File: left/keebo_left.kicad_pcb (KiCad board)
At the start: 2 copper layers, 152.4 x 100 mm, 58 parts, among them J1 Conn_01x05, J2 Conn_01x08, SW1 SW_Push, SW10 SW_Push, SW11 SW_Push, SW12 SW_Push, SW13 SW_Push, SW14 SW_Push, SW17 SW_Push, SW18 SW_Push, SW19 SW_Push, SW2 SW_Push, SW20 SW_Push, SW21 SW_Push, SW22 SW_Push, SW25 SW_Push, SW26 SW_Push, SW27 SW_Push, SW28 SW_Push, SW29 SW_Push, SW3 SW_Push, SW30 SW_Push, SW35 SW_Push, SW36 SW_Push, SW37 SW_Push, SW4 SW_Push, SW5 SW_Push, SW6 SW_Push, SW7 SW_Push, SW9 SW_Push

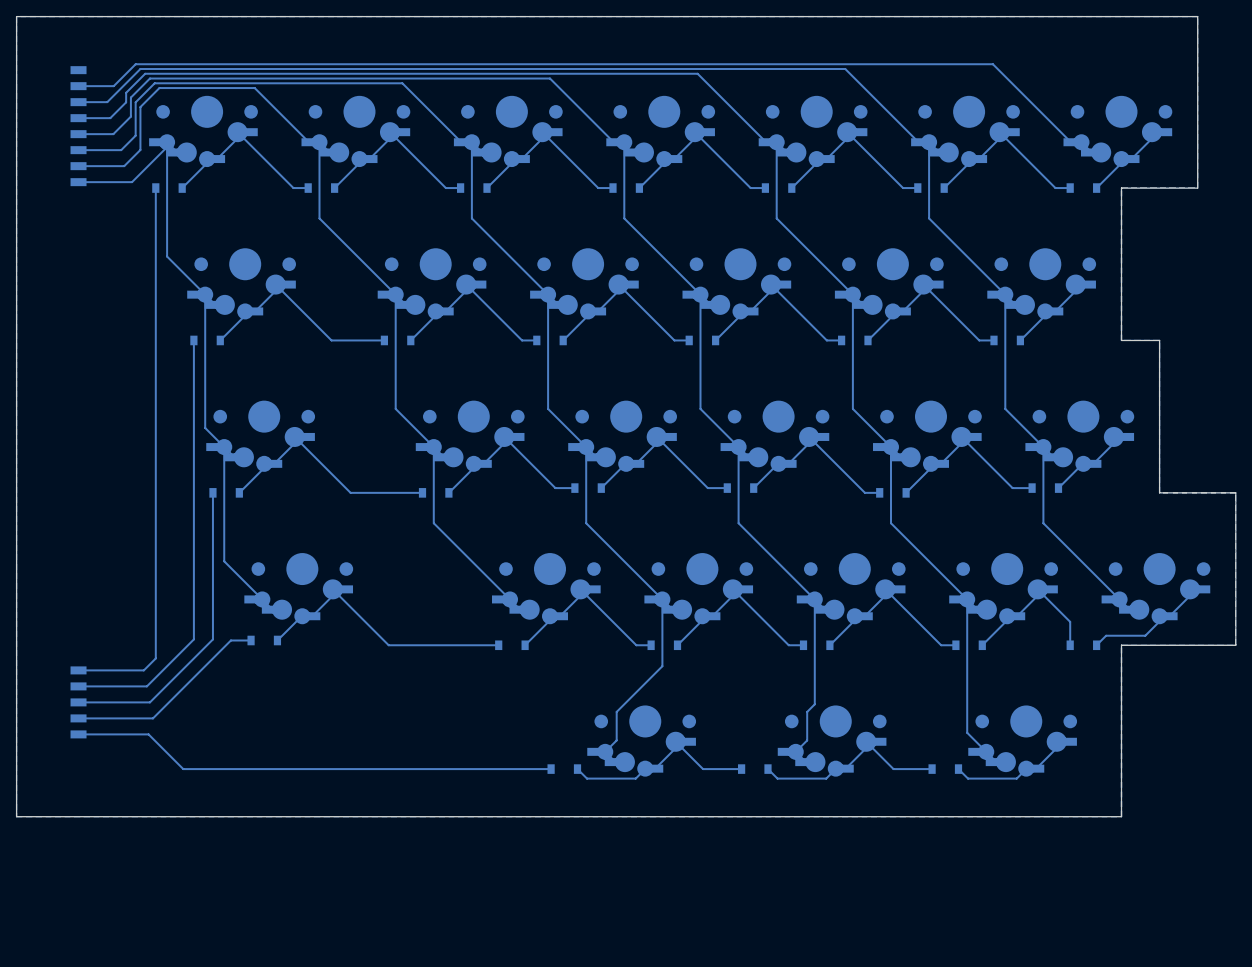
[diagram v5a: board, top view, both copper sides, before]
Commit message: Fix key matrix; use MX exclusively; Fix MX missing side holes.
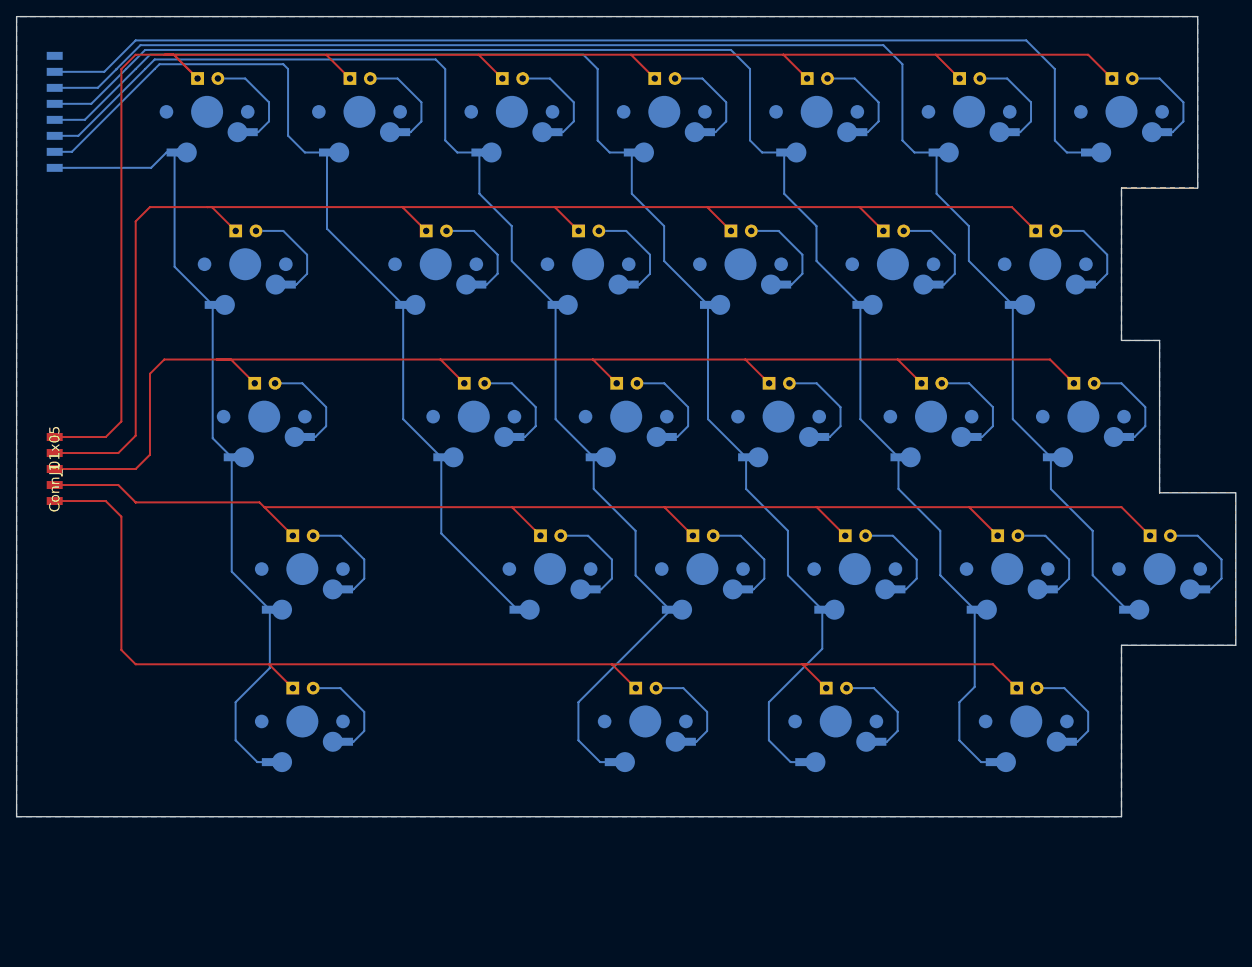
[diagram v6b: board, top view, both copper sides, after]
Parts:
- added D33: 1N4148, Diodes_THT:D_DO-35_SOD27_P2.54mm_Vertical_AnodeUp, B.Cu at (53.6, 103.0)
- added SW33: SW_Push, kbo_mx_3d:KeeboHR_125_MX, B.Cu at (54.8, 107.2)
- D1, D10, D11, D12, D13, D14, D17, D18, D19, D2, D20, D21, D22, D25, D26, D27, D28, D29, D3, D30, D35, D36, D37, D4, D5, D6, D7, D9: footprint Diodes_SMD:D_SOD-123 -> Diodes_THT:D_DO-35_SOD27_P2.54mm_Vertical_AnodeUp
- J1: moved to F.Cu
- SW1, SW10, SW11, SW12, SW13, SW14, SW18, SW19, SW2, SW20, SW21, SW22, SW26, SW27, SW28, SW29, SW3, SW30, SW4, SW5, SW6, SW7: footprint kbo_mx_lp_3d:KeeboHR_100_MX_LP -> kbo_mx_3d:KeeboHR_100_MX
- SW17: footprint kbo_mx_lp_3d:KeeboHR_175_MX_LP -> kbo_mx_3d:KeeboHR_175_MX
- SW25: footprint kbo_mx_lp_3d:KeeboHR_225_MX_LP -> kbo_mx_3d:KeeboHR_225_MX
- SW35, SW36, SW37: footprint kbo_mx_lp_3d:KeeboHR_125_MX_LP -> kbo_mx_3d:KeeboHR_125_MX
- SW9: footprint kbo_mx_lp_3d:KeeboHR_150_MX_LP -> kbo_mx_3d:KeeboHR_150_MX
- moved J1 29.3 mm to (23.8, 75.6)
- moved D30 16.0 mm to (160.7, 83.9)
- moved D1 14.2 mm to (41.7, 26.8)
- moved D2 14.2 mm to (60.7, 26.8)
- moved D3 14.2 mm to (79.8, 26.8)
- moved D5 14.2 mm to (117.9, 26.8)
- moved D6 14.2 mm to (136.9, 26.8)
- moved D7 14.2 mm to (156.0, 26.8)
- moved D4 14.2 mm to (98.8, 26.8)
- moved D11 14.2 mm to (89.3, 45.8)
- moved D12 14.2 mm to (108.3, 45.8)
- moved D13 14.2 mm to (127.4, 45.8)
- moved D14 14.2 mm to (146.4, 45.8)
- moved D17 14.2 mm to (48.8, 64.9)
- moved D9 14.2 mm to (46.4, 45.8)
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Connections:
- D10 pad 1: Net-(D10-Pad1) -> /row2
- D11 pad 1: Net-(D10-Pad2) -> /row2
- D12 pad 1: Net-(D11-Pad2) -> /row2
- D13 pad 1: Net-(D12-Pad2) -> /row2
- D14 pad 1: Net-(D13-Pad2) -> /row2
- D18 pad 1: Net-(D17-Pad2) -> /row3
- D19 pad 1: Net-(D18-Pad2) -> /row3
- D2 pad 1: Net-(D1-Pad2) -> /row1
- D20 pad 1: Net-(D19-Pad2) -> /row3
- D21 pad 1: Net-(D20-Pad2) -> /row3
- D22 pad 1: Net-(D21-Pad2) -> /row3
- D26 pad 1: Net-(D25-Pad2) -> /row4
- D27 pad 1: Net-(D26-Pad2) -> /row4
- D28 pad 1: Net-(D27-Pad2) -> /row4
- D29 pad 1: Net-(D28-Pad2) -> /row4
- D3 pad 1: Net-(D2-Pad2) -> /row1
- D30 pad 1: Net-(D29-Pad2) -> /row4
- D36 pad 1: Net-(D35-Pad2) -> /row5
- D37 pad 1: Net-(D36-Pad2) -> /row5
- D4 pad 1: Net-(D3-Pad2) -> /row1
- D5 pad 1: Net-(D4-Pad2) -> /row1
- D6 pad 1: Net-(D5-Pad2) -> /row1
- D7 pad 1: Net-(D6-Pad2) -> /row1
- D9 pad 2: Net-(D10-Pad1) -> Net-(D9-Pad2)
- SW9 pad 1: Net-(D10-Pad1) -> Net-(D9-Pad2)
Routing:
- net /row1: track 69.1 -> 210.8 mm
- net /row4: track 25.6 -> 164.8 mm
- net /row3: track 38.4 -> 163.1 mm
- net /row2: track 54.2 -> 173.9 mm
- net /row5: track 60.9 -> 152.9 mm
- net Net-(D10-Pad1): track 28.6 -> 0.00 mm
- net /col1: track 92.5 -> 117.5 mm
- net Net-(D25-Pad2): track 35.2 -> 13.0 mm
- net Net-(D17-Pad2): track 31.0 -> 14.5 mm
- net Net-(D9-Pad2): track 0.00 -> 14.5 mm
- net Net-(D33-Pad2): track 0.00 -> 14.5 mm
- net Net-(D36-Pad2): track 26.9 -> 13.0 mm
- net Net-(D35-Pad2): track 26.9 -> 13.0 mm
- net Net-(D4-Pad2): track 23.8 -> 14.5 mm
- net Net-(D1-Pad2): track 25.4 -> 16.0 mm
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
